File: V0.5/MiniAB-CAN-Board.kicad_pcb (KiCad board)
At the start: 4 copper layers, 155.2 x 57.2 mm, 127 parts, among them J1 PCF, J10 USB_B_Micro, J11 CAN, J12 ENDSTOP1, J13 ENDSTOP2, J14 PROBE, J2 PCF, J3 HEF, J4 TH0, J6 H0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

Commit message: Update V0.5
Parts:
- C25, C31, C39, C42, C43, C44: moved to B.Cu
- J9: footprint Connector_PinHeader_1.27mm:PinHeader_1x05_P1.27mm_Vertical_SMD_Pin1Left -> Connector_PinHeader_1.27mm:PinHeader_1x05_P1.27mm_Vertical; moved to F.Cu
- SW1, SW2: moved to F.Cu
- moved J9 137.3 mm to (108.4, 82.8), turned to 90 degrees
- moved D5 127.2 mm to (91.3, 56.8)
- moved D4 127.2 mm to (90.9, 52.9)
- moved R13 127.2 mm to (87.0, 54.5)
- moved R16 127.2 mm to (93.3, 57.6)
- moved R17 127.2 mm to (80.9, 52.5)
- moved R20 127.2 mm to (82.9, 54.4)
- moved D6 127.2 mm to (83.0, 52.9)
- moved D7 127.2 mm to (84.9, 54.0)
- moved R10 125.9 mm to (100.4, 92.3), turned to 0 degrees
- moved R8 125.5 mm to (100.7, 84.4)
- moved R9 124.3 mm to (100.7, 83.5), turned to 0 degrees
- moved D3 122.4 mm to (102.2, 92.3), turned to 180 degrees
- moved SW2 82.3 mm to (107.5, 78.9), turned to 0 degrees
- moved R29 80.1 mm to (110.8, 81.0), turned to 180 degrees
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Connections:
- net CANH renamed CAN+
- net VBAT renamed +3V3
- J11 pad 1: CANL -> PWR
- J11 pad 2: PWR -> GND
- J11 pad 4: GND -> CAN-
- R27 pad 1: CANL -> CAN-
- U1 pad 8: ADXL_INT1 -> unconnected-(U1-Pad8)
- U8 pad 6: CANL -> CAN-
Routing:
- net NEOPIXEL: track 0.00 -> 3.50 mm
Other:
- board size 155.2 x 57.2 mm -> 51 x 43.3 mm
- board text removed: "24V"
- board text removed: "3V3"
- board text removed: "5V"
- board text removed: "A1"
- board text removed: "A2"
- board text removed: "B1"
- board text removed: "B2"
- board text removed: "BOOT1"
- board text removed: "CANH"
- board text removed: "CANL"
- board text removed: "GND"
- board text removed: "NRST"
- board text removed: "PA10"
- board text removed: "PA9"
- board text removed: "PB0"
- board text removed: "PB1"
- board text removed: "PB12"
- board text removed: "PB13"
- board text removed: "PB15"
- board text removed: "SCL"
- board text removed: "SDA"
- board text removed: "SWCLK"
- board text removed: "SWDIO"
- board text removed: "V+"

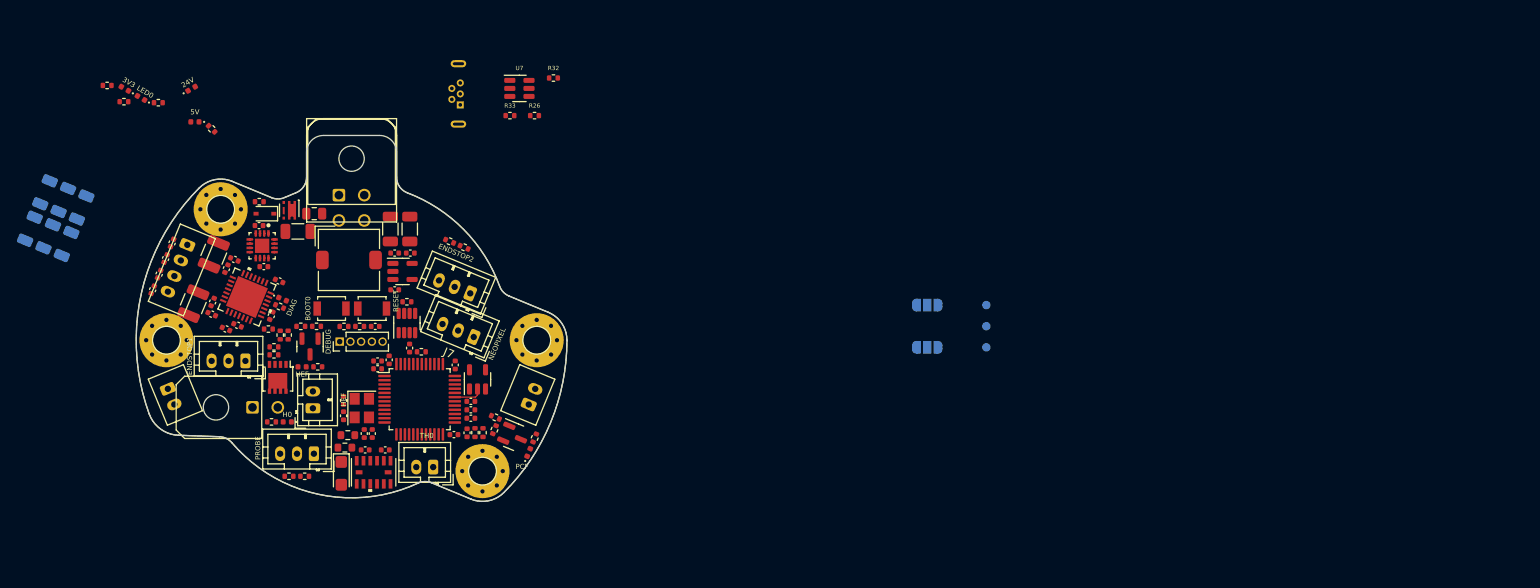
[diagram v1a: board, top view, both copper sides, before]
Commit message: JNP Layout and first routings
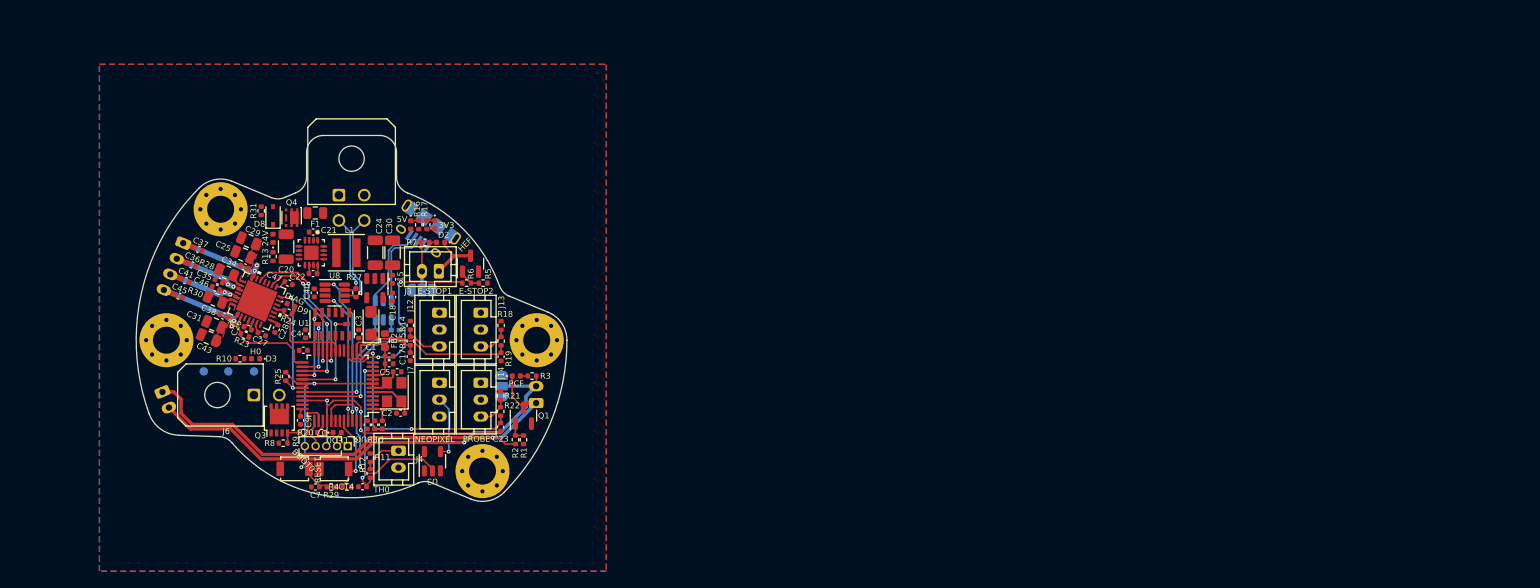
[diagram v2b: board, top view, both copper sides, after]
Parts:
- removed C16: 1u, Capacitor_SMD:C_0402_1005Metric
- removed C39, C42, C44: 10u/35V, Capacitor_SMD:C_1206_3216Metric
- removed FB1: GZ1608D601TF, Resistor_SMD:R_0603_1608Metric
- added C29: 10u/35V, Capacitor_SMD:C_0805_2012Metric, F.Cu at (97.7, 70.9)
- C15: value 1u -> 2u2
- C25, C31, C43: footprint Capacitor_SMD:C_1206_3216Metric -> Capacitor_SMD:C_0805_2012Metric; moved to F.Cu
- J10: footprint Connector_USB:USB_Micro-B_Wuerth_614105150721_Vertical -> Connector_USB:USB_Micro-B_Amphenol_10118194_Horizontal
- J12: value ENDSTOP1 -> E-STOP1
- J13: value ENDSTOP2 -> E-STOP2
- L1: footprint Inductor_SMD:L_TDK_SLF7045 -> Inductor_SMD:L_Coilcraft_XxL4020
- R26, R32, R33, U7: moved to B.Cu
- R28, R30: footprint Resistor_SMD:R_1210_3225Metric -> Resistor_SMD:R_0805_2012Metric
- moved TP2 92.8 mm to (92.3, 86.3), turned to 0 degrees
- moved TP4 90.1 mm to (95.2, 86.3), turned to 0 degrees
- moved TP3 86.7 mm to (98.3, 86.3)
- moved JP2 59.9 mm to (118.2, 76.7)
- moved JP1 50.6 mm to (127.6, 88.1), turned to -90 degrees
- moved D7 45.9 mm to (108.2, 93.6), turned to 0 degrees
- moved R20 45.6 mm to (106.3, 93.6)
- moved R17 41.3 mm to (118.8, 69.0), turned to -90 degrees
- moved D6 40.1 mm to (119.7, 69.0), turned to -90 degrees
- moved R32 35.9 mm to (114.6, 82.0), turned to 90 degrees
- moved U7 30.8 mm to (113.6, 79.1), turned to 90 degrees
- moved R26 30.5 mm to (115.5, 82.0), turned to 90 degrees
- moved R33 30.4 mm to (112.7, 82.0), turned to 90 degrees
- moved D5 28.3 mm to (116.8, 69.0), turned to -90 degrees
- moved R16 27.0 mm to (117.8, 69.0), turned to -90 degrees
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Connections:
- net TMC_VS renamed +24V
- net VDDA renamed +3.3VA
- C1 pad 1: Net-(C1-Pad1) -> +3V3
- C3 pad 1: Net-(C1-Pad1) -> +3V3
- H1 pad 1: GND -> unconnected-(H1-Pad1)
- H2 pad 1: GND -> unconnected-(H2-Pad1)
- H3 pad 1: GND -> unconnected-(H3-Pad1)
- H4 pad 1: GND -> unconnected-(H4-Pad1)
- J10 pad 1: Net-(J10-Pad1) -> +5V
- R26 pad 2: +3V3 -> +5V
- U1 pad 6: Net-(C1-Pad1) -> +3V3
- U2 pad 10: unconnected-(U2-Pad10) -> TH0
- U2 pad 11: LED0 -> unconnected-(U2-Pad11)
- U2 pad 13: ADXL_INT1 -> ENDSTOP1
- U2 pad 14: ADXL_CS -> ENDSTOP2
- U2 pad 15: SCLK -> PROBE
- U2 pad 16: SDO -> HE-FAN
- U2 pad 17: SDI -> unconnected-(U2-Pad17)
- U2 pad 18: HE-FAN -> unconnected-(U2-Pad18)
- U2 pad 19: TH0 -> ST_DIAG
- U2 pad 2: ST_ENN -> unconnected-(U2-Pad2)
- U2 pad 20: BOOT1 -> unconnected-(U2-Pad20)
- U2 pad 21: SCL -> ST_DIR
- U2 pad 22: SDA -> ST_STEP
- U2 pad 25: PC-FAN -> ST_ENN
- U2 pad 26: ENDSTOP2 -> SCLK
- U2 pad 27: unconnected-(U2-Pad27) -> SDO
- U2 pad 28: ENDSTOP1 -> SDI
- U2 pad 29: unconnected-(U2-Pad29) -> ADXL_CS
- U2 pad 30: PROBE -> ST_TX
- U2 pad 31: NEOPIXEL -> ST_RX
- U2 pad 38: ST_DIAG -> HEATER
- U2 pad 39: ST_DIR -> LED0
- U2 pad 40: ST_STEP -> PC-FAN
- U2 pad 41: HEATER -> NEOPIXEL
- U2 pad 42: ST_TX -> SCL
- U2 pad 43: ST_RX -> SDA
- U7 pad 5: Net-(J10-Pad1) -> +5V
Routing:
- net Net-(D1-Pad1): track 0.00 -> 56.9 mm, vias 0 -> 1
- net Net-(J1-Pad2): track 0.00 -> 55.6 mm, vias 0 -> 1
- net PROBE: track 0.00 -> 28.5 mm, vias 0 -> 2
- net PC-FAN: track 0.00 -> 28.0 mm, vias 0 -> 2
- net HE-FAN: track 0.00 -> 23.9 mm, vias 0 -> 2
- net RESET: track 0.00 -> 22.3 mm, vias 0 -> 2
- net ENDSTOP2: track 0.00 -> 19.8 mm
- net NEOPIXEL: track 3.50 -> 22.5 mm, vias 0 -> 2
- net ST_DIR: track 0.00 -> 18.5 mm, vias 0 -> 2
- net CAN_TX: track 0.00 -> 18.1 mm, vias 0 -> 2
- net USB_DP: track 0.00 -> 16.8 mm, vias 0 -> 1
- net CAN_RX: track 0.00 -> 16.0 mm, vias 0 -> 2
- net TH0: track 0.00 -> 15.8 mm, vias 0 -> 2
- net ST_STEP: track 0.00 -> 15.8 mm, vias 0 -> 2
- net ST_RX: track 0.00 -> 14.4 mm, vias 0 -> 2
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- added copper zone on F.Cu, net +24V
- added copper zone on In1.Cu, net +3V3
- added copper zone on F.Cu, net A1
- added copper zone on F.Cu, net A2
- added copper zone on F.Cu, net B1
- added copper zone on F.Cu, net B2
- added copper zone on B.Cu, net GND
- added copper zone on F.Cu, net GND
- added copper zone on In2.Cu, net GND

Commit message: Routing finished
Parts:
- moved TP2 33.1 mm to (124.0, 76.7)
- moved TP4 32.7 mm to (126.5, 76.7)
- moved JP1 30.3 mm to (97.5, 91.8), turned to 180 degrees
- moved TP3 25.1 mm to (121.5, 76.7)
- moved R10 6.77 mm to (98.0, 91.5), turned to -90 degrees
- moved D3 6.64 mm to (98.9, 91.5), turned to 90 degrees
- moved U7 3.77 mm to (113.6, 75.3)
- moved R26 3.66 mm to (115.5, 78.3)
- moved R32 3.66 mm to (114.6, 78.3)
- moved R33 3.66 mm to (112.7, 78.3)
- moved J6 2.84 mm to (97.3, 86.5), turned to 112.5 degrees
- moved R25 1.22 mm to (102.6, 88.0)
- moved Q1 0.63 mm to (129.7, 91.9)
- moved R1 0.63 mm to (129.7, 94.8)
- moved R2 0.63 mm to (128.7, 94.8)
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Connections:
- net Net-(J10-Pad2) renamed /D-
- net Net-(J10-Pad3) renamed /D+
- net USB_DM renamed USB_D-
- net USB_DP renamed USB_D+
- J11 pad 3: CAN+ -> CAN-
- J11 pad 4: CAN- -> CAN+
- U2 pad 19: ST_DIAG -> ST_DIR
- U2 pad 21: ST_DIR -> ST_DIAG
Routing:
- net +5V: track 0.00 -> 75.6 mm, vias 0 -> 4
- net +24V: track 0.00 -> 64.4 mm, vias 0 -> 23
- net +3V3: track 6.40 -> 35.0 mm, vias 0 -> 21
- net GND: track 0.00 -> 15.2 mm, vias 0 -> 119
- net Net-(J1-Pad2): track 55.6 -> 63.0 mm
- net HE-FAN: track 23.9 -> 19.2 mm
- net USB_D-: track 13.6 -> 17.8 mm
- net PWR: track 0.00 -> 3.52 mm
- net ST_STEP: track 15.8 -> 19.1 mm
- net Net-(D8-Pad2): track 0.00 -> 3.11 mm
- net USB_D+: track 16.8 -> 19.6 mm
- net ST_DIR: track 18.5 -> 21.1 mm
- net Net-(D3-Pad1): track 0.00 -> 2.48 mm
- net /D-: track 10.2 -> 7.79 mm
- net /D+: track 9.56 -> 7.46 mm
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- added copper zone on F.Cu, net +3V3
- added copper zone on F.Cu, net +5V
- added copper zone on F.Cu, net Net-(C22-Pad1)
- added copper zone on F.Cu, net Net-(D3-Pad1)

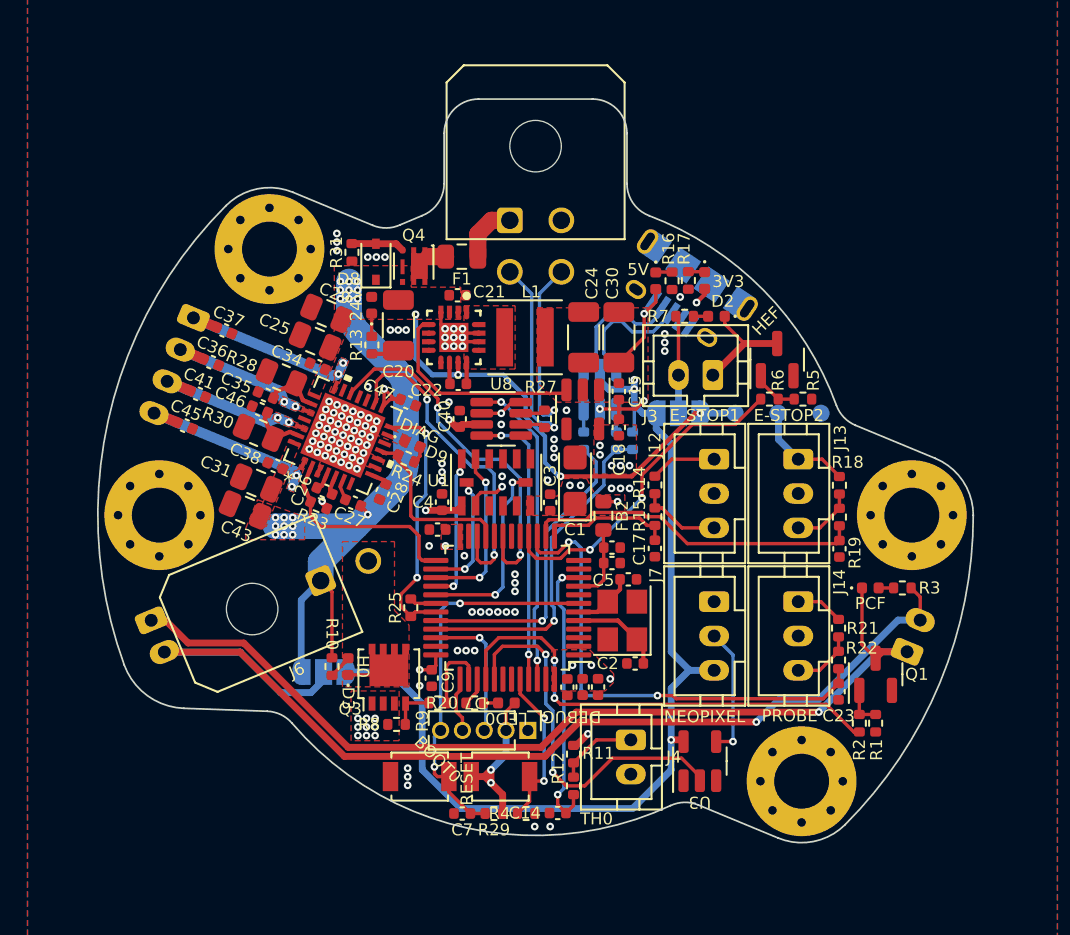
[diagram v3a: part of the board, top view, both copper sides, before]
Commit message: Add vias to board edge
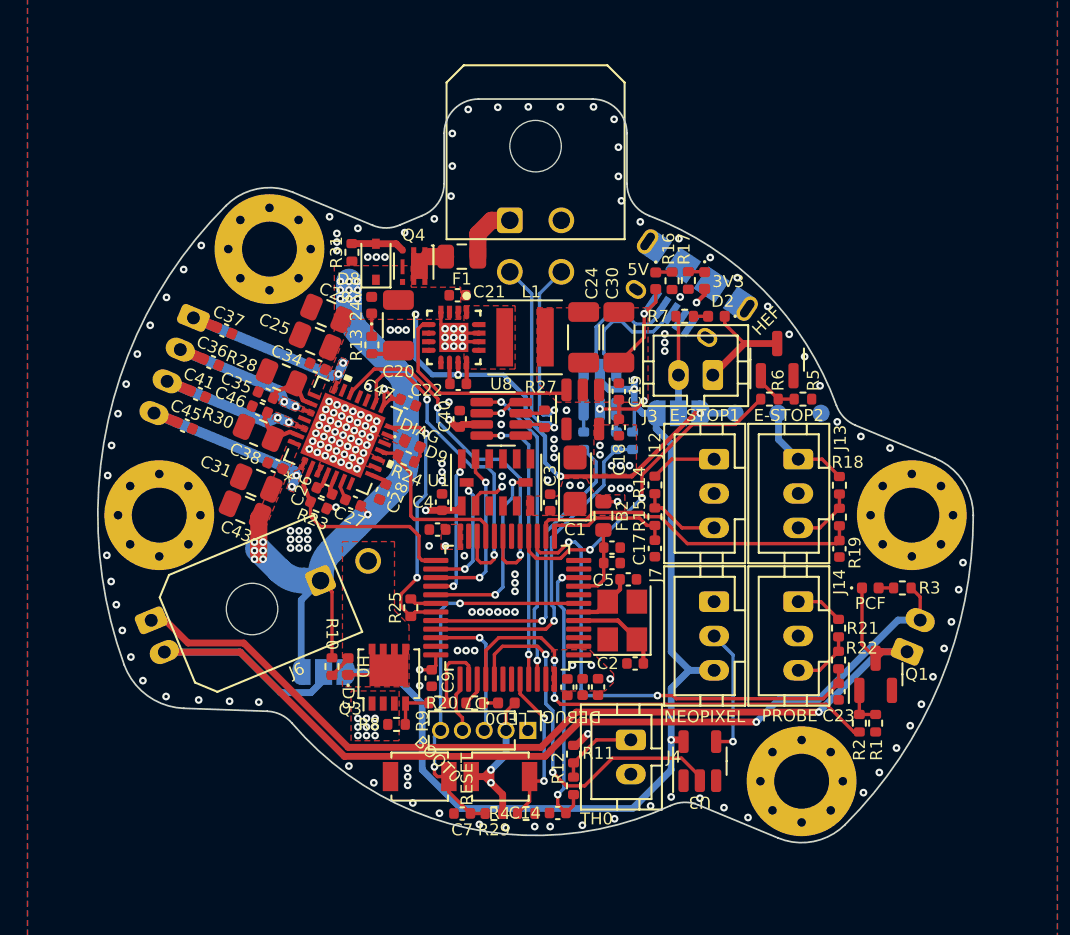
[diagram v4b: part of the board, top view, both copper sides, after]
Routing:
- net +24V: track 64.4 -> 66.2 mm, vias 23 -> 20
- net GND: vias 119 -> 197

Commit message: Update routing
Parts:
- moved D5 2.74 mm to (119.6, 69.0), turned to -124 degrees
- moved R16 2.64 mm to (120.4, 69.6), turned to 56 degrees
- moved R17 1.47 mm to (117.8, 67.8), turned to 56 degrees
- moved D6 1.25 mm to (118.6, 68.4), turned to 56 degrees
- moved R26 1.13 mm to (115.4, 79.5)
- moved R32 1.13 mm to (114.5, 79.5)
- moved R33 1.13 mm to (112.6, 79.5)
- moved U7 1.13 mm to (113.5, 76.5)
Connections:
- U2 pad 15: PROBE -> HE-FAN
- U2 pad 16: HE-FAN -> PROBE
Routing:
- net +5V: track 75.6 -> 93.0 mm, vias 4 -> 5
- net +24V: track 66.2 -> 82.4 mm, vias 20 -> 11
- net GND: track 15.2 -> 17.2 mm, vias 197 -> 116
- net +3V3: track 35.0 -> 36.7 mm, vias 21 -> 17
- net PROBE: track 28.5 -> 27.5 mm
- net HE-FAN: track 19.2 -> 18.3 mm

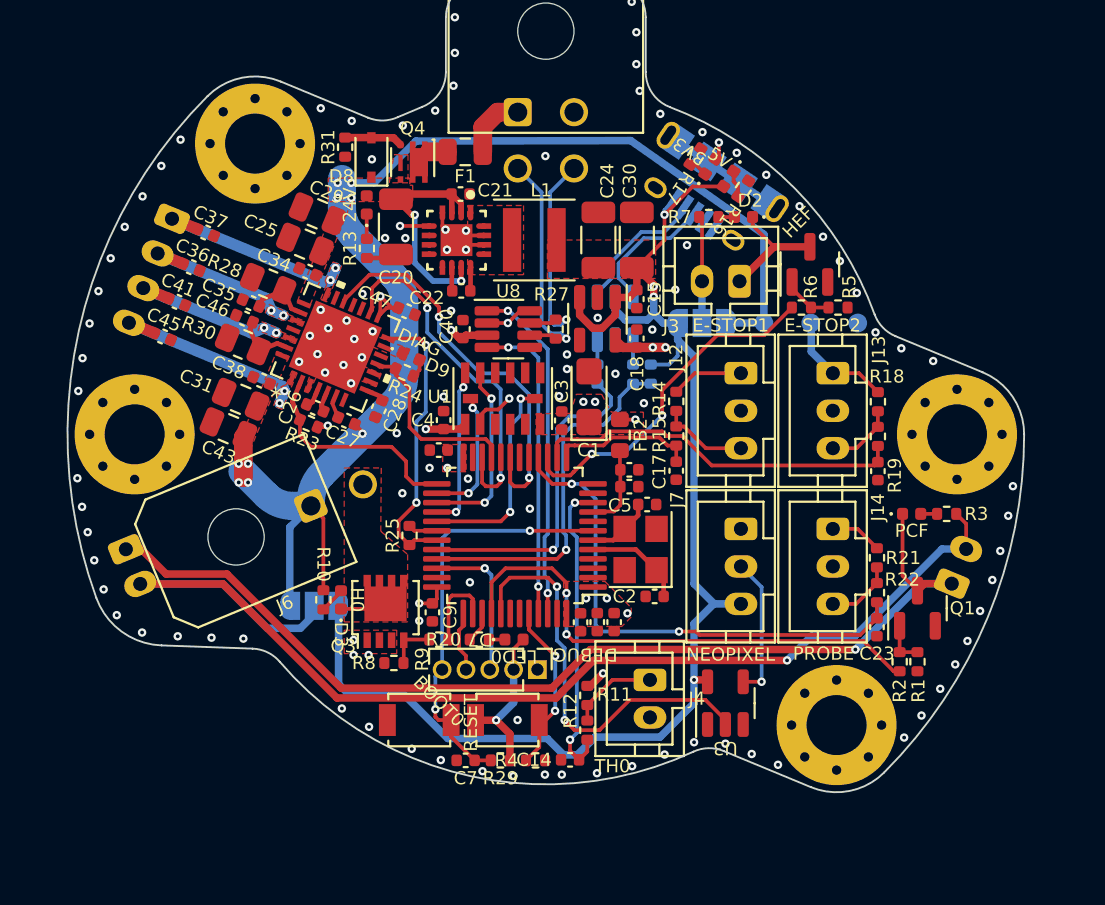
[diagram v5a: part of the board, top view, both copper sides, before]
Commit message: Update silk screen
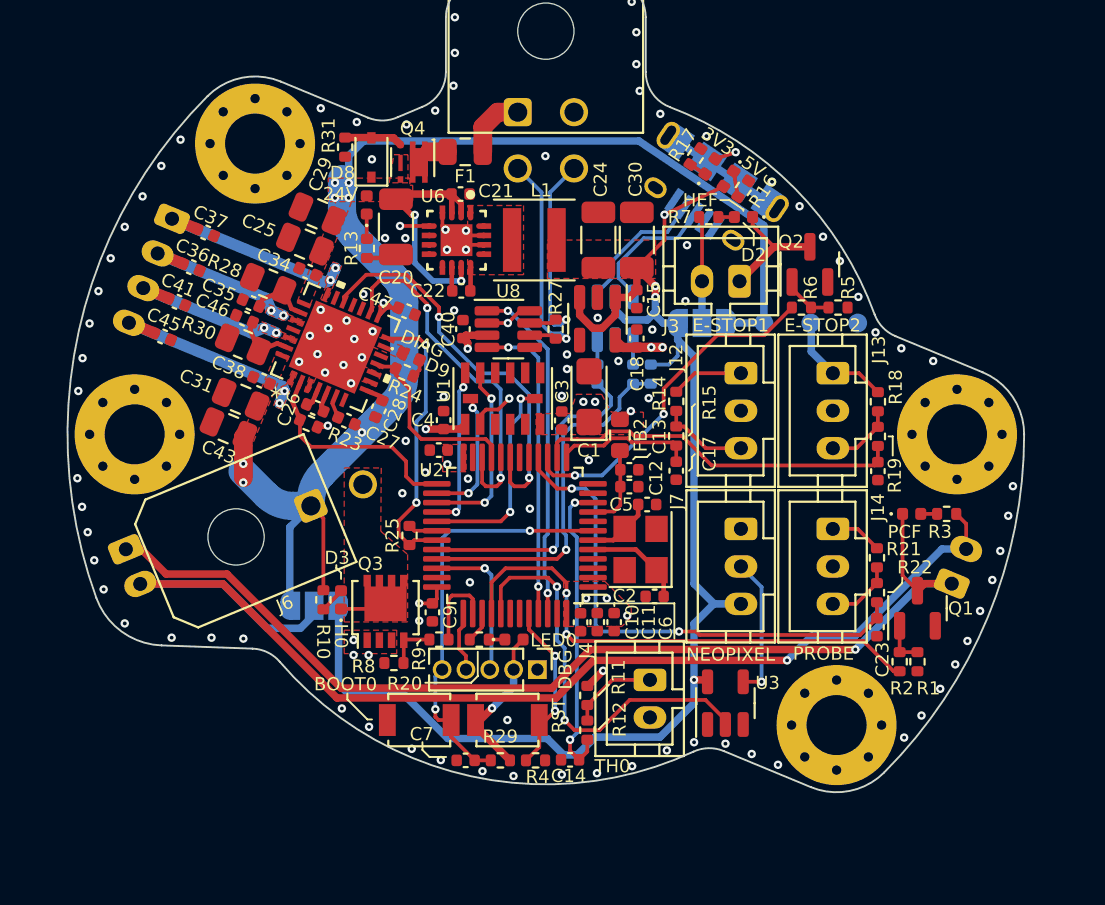
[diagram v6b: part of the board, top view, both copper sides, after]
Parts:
- J9: value DEBUG -> DBG
- SW1: value RESET -> RST
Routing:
- net +24V: track 82.4 -> 83.5 mm, vias 11 -> 9
- net +3V3: track 36.7 -> 35.9 mm
- net GND: vias 116 -> 114
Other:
- board text added: "24V"
- board text added: "3V3"
- board text added: "5V"
- board text added: "CANH"
- board text added: "CANL"
- board text added: "GND"
- board text added: "PA0"
- board text added: "PA15"
- board text added: "PA3"
- board text added: "PA4"
- board text added: "PA5"
- board text added: "PA6"
- board text added: "PB5"
- board text added: "RESET"
- board text added: "SWCLK"
- board text added: "SWDIO"
- board text added: "V+"

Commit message: Update silkscreen
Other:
- board text added: "MiniAB CAN Board"
- board text added: "V0.5"
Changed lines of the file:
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@@
     (effects (font (size 0.7 0.7) (thickness 0.1)) (justify mirror))
+  )
+  (gr_text "MiniAB CAN Board" (at 108.17 86.78) (layer "B.SilkS")
+    (effects (font (size 1.4 1.4) (thickness 0.2)) (justify mirror))
   )
   (gr_text "SWDIO" (at 106.86 92.7 270) (layer "B.SilkS")
@@
     (effects (font (size 0.7 0.7) (thickness 0.1)) (justify mirror))
   )
+  (gr_text "V0.5" (at 99.94 88.69) (layer "B.SilkS")
+    (effects (font (size 0.7 0.7) (thickness 0.1)) (justify mirror))
+  )
